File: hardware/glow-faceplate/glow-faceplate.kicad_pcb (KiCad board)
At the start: 2 copper layers, 80.9 x 68 mm, 15 parts

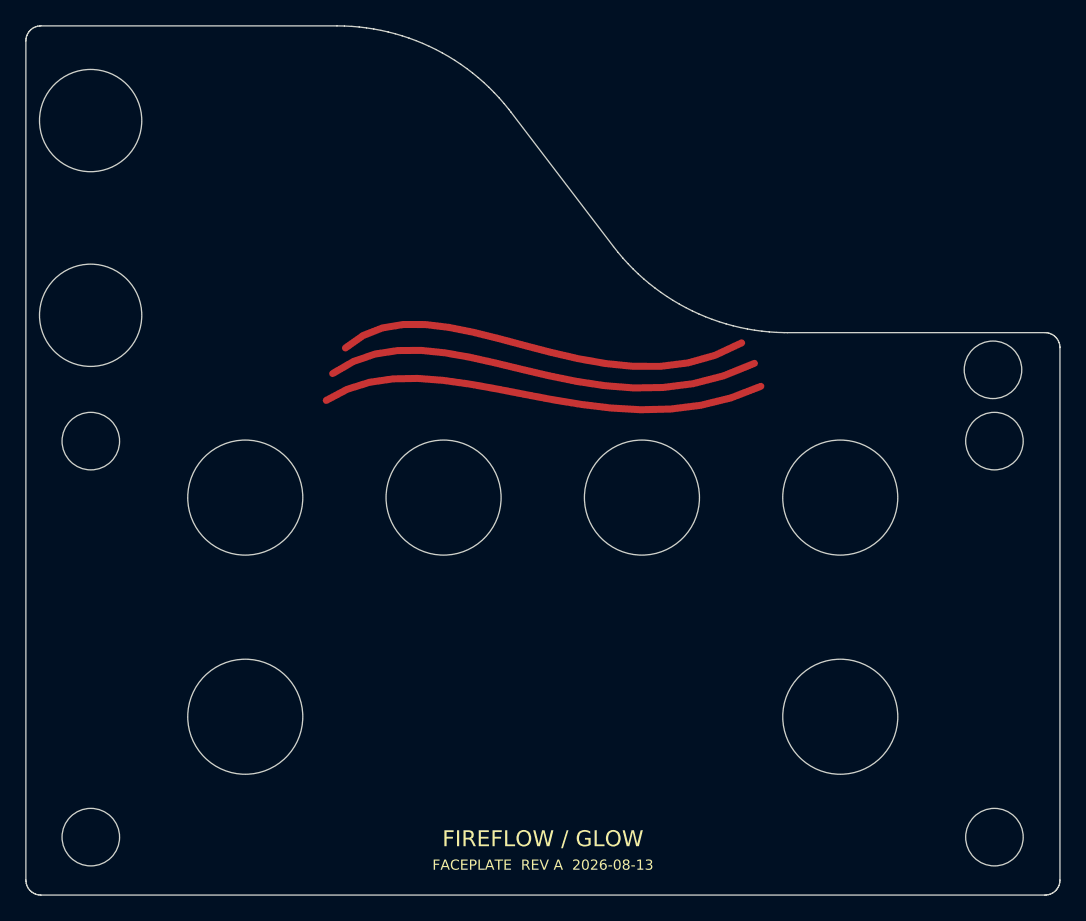
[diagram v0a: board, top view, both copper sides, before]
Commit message: fix(glow): derive faceplate mechanics from pinned DXF
Co-Authored-By: HAL 9000 <293417720+bea-ton-k@users.noreply.github.com>
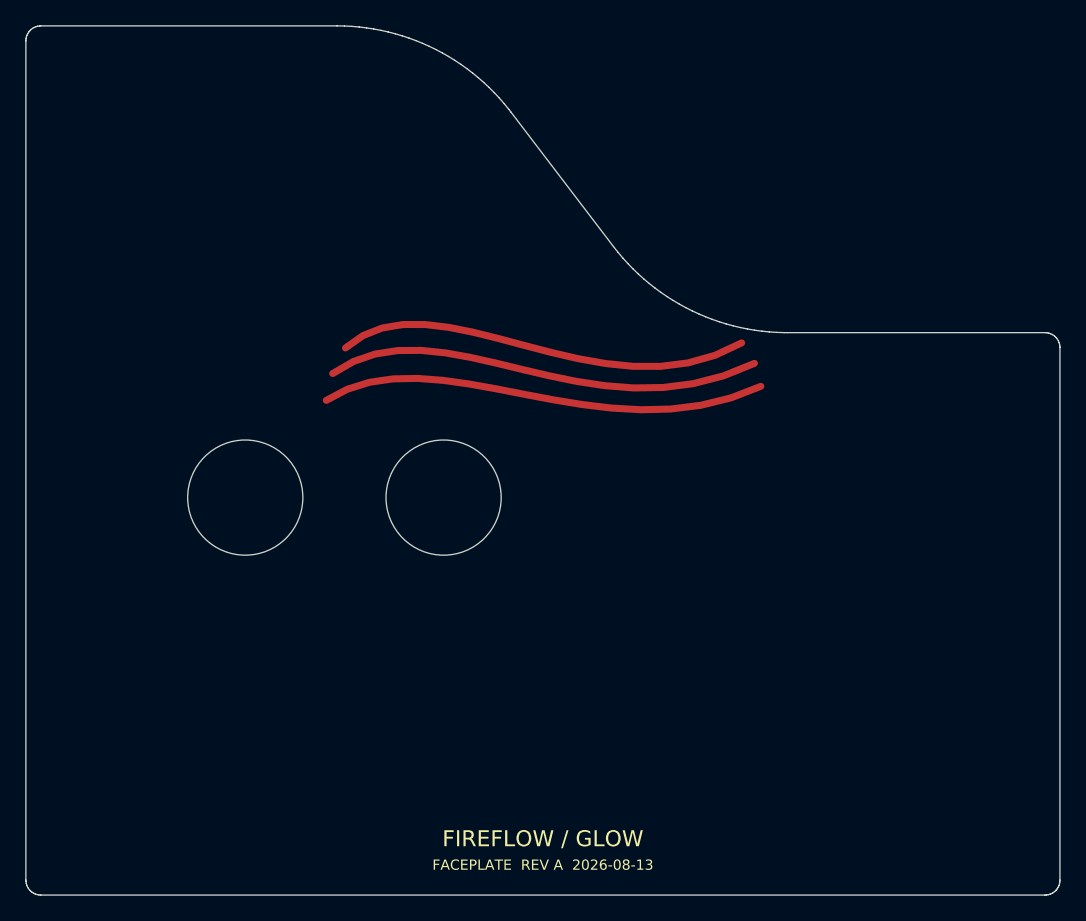
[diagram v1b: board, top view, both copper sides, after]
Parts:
- removed FADER_LEFT, FADER_RIGHT: NPTH SLOT 4.301 x 26.0409 mm, Glow_NPTH_SLOT_4.301x26.0409mm
- removed JACK_LOWER, JACK_UPPER: NPTH 8 mm, Glow_NPTH_8mm
- removed KNOB_1, KNOB_2, KNOB_3, KNOB_4, KNOB_5, KNOB_6: NPTH 9 mm, Glow_NPTH_9mm
- removed MOUNT_FADER_L_BOTTOM, MOUNT_FADER_L_TOP, MOUNT_FADER_R_BOTTOM, MOUNT_FADER_R_TOP, MOUNT_UPPER_RIGHT: NPTH 4.5 mm, Glow_NPTH_4.5mm
- added DXF_00: DXF NPTH 4.510605 x 4.528 mm, Glow_DXF_NPTH_DXF_00, F.Cu at (5.08, 32.5)
- added DXF_01_13_17: DXF NPTH 4.300995 x 26.0409 mm, Glow_DXF_NPTH_DXF_01_13_17, F.Cu at (5.08, 48.0)
- added DXF_02_12: DXF NPTH 9.010597 x 9.010597 mm, Glow_DXF_NPTH_DXF_02_12, F.Cu at (17.2, 36.9)
- added DXF_03_11: DXF NPTH 9.010597 x 9.010597 mm, Glow_DXF_NPTH_DXF_03_11, F.Cu at (32.7, 36.9)
- added DXF_04_10: DXF NPTH 9.010604 x 9.010601 mm, Glow_DXF_NPTH_DXF_04_10, F.Cu at (48.2, 36.8)
- added DXF_05_07_09: DXF NPTH 9.010604 x 9.010597 mm, Glow_DXF_NPTH_DXF_05_07_09, F.Cu at (63.7, 36.9)
- added DXF_06: DXF NPTH 4.510605 x 4.528 mm, Glow_DXF_NPTH_DXF_06, F.Cu at (75.8, 32.5)
- added DXF_08: DXF NPTH 4.300995 x 26.0409 mm, Glow_DXF_NPTH_DXF_08, F.Cu at (75.8, 48.0)
- added DXF_14_16: DXF NPTH 9.010597 x 9.010601 mm, Glow_DXF_NPTH_DXF_14_16, F.Cu at (17.2, 54.0)
- added DXF_15: DXF NPTH 9.010604 x 9.010601 mm, Glow_DXF_NPTH_DXF_15, F.Cu at (63.7, 54.0)
- added DXF_18: DXF NPTH 4.510605 x 4.528 mm, Glow_DXF_NPTH_DXF_18, F.Cu at (5.08, 63.5)
- added DXF_21: DXF NPTH 4.510605 x 4.528 mm, Glow_DXF_NPTH_DXF_21, F.Cu at (75.8, 63.5)
- added DXF_23: DXF NPTH 8.010597 x 8.0107 mm, Glow_DXF_NPTH_DXF_23, F.Cu at (5.07, 7.41)
- added DXF_24: DXF NPTH 8.010597 x 8.010702 mm, Glow_DXF_NPTH_DXF_24, F.Cu at (5.07, 22.6)
- added DXF_25: DXF NPTH 4.510589 x 4.510601 mm, Glow_DXF_NPTH_DXF_25, F.Cu at (75.7, 26.9)

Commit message: fix(glow): route exact DXF aperture contours
Co-Authored-By: HAL 9000 <293417720+bea-ton-k@users.noreply.github.com>
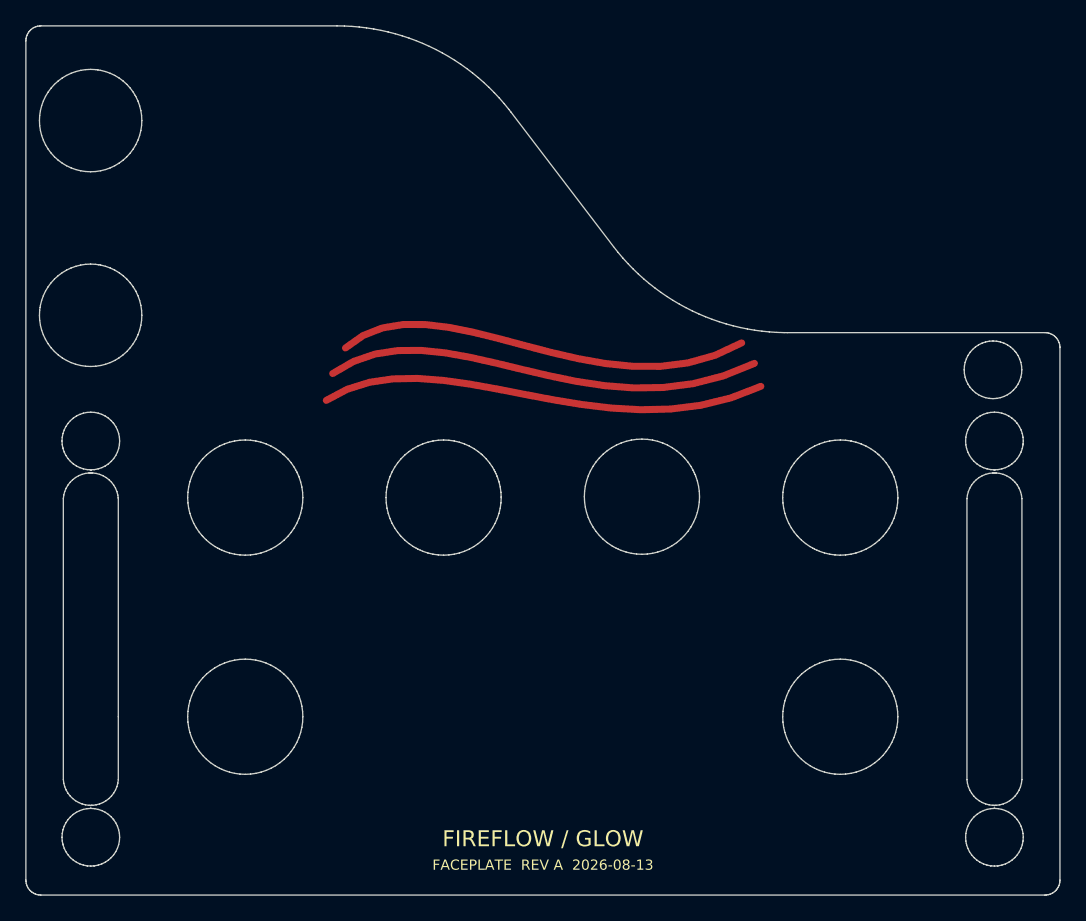
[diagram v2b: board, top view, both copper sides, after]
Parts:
- removed DXF_00: DXF NPTH 4.510605 x 4.528 mm, Glow_DXF_NPTH_DXF_00
- removed DXF_01_13_17: DXF NPTH 4.300995 x 26.0409 mm, Glow_DXF_NPTH_DXF_01_13_17
- removed DXF_02_12: DXF NPTH 9.010597 x 9.010597 mm, Glow_DXF_NPTH_DXF_02_12
- removed DXF_03_11: DXF NPTH 9.010597 x 9.010597 mm, Glow_DXF_NPTH_DXF_03_11
- removed DXF_04_10: DXF NPTH 9.010604 x 9.010601 mm, Glow_DXF_NPTH_DXF_04_10
- removed DXF_05_07_09: DXF NPTH 9.010604 x 9.010597 mm, Glow_DXF_NPTH_DXF_05_07_09
- removed DXF_06: DXF NPTH 4.510605 x 4.528 mm, Glow_DXF_NPTH_DXF_06
- removed DXF_08: DXF NPTH 4.300995 x 26.0409 mm, Glow_DXF_NPTH_DXF_08
- removed DXF_14_16: DXF NPTH 9.010597 x 9.010601 mm, Glow_DXF_NPTH_DXF_14_16
- removed DXF_15: DXF NPTH 9.010604 x 9.010601 mm, Glow_DXF_NPTH_DXF_15
- removed DXF_18: DXF NPTH 4.510605 x 4.528 mm, Glow_DXF_NPTH_DXF_18
- removed DXF_21: DXF NPTH 4.510605 x 4.528 mm, Glow_DXF_NPTH_DXF_21
- removed DXF_23: DXF NPTH 8.010597 x 8.0107 mm, Glow_DXF_NPTH_DXF_23
- removed DXF_24: DXF NPTH 8.010597 x 8.010702 mm, Glow_DXF_NPTH_DXF_24
- removed DXF_25: DXF NPTH 4.510589 x 4.510601 mm, Glow_DXF_NPTH_DXF_25
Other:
- outline, holes or cut-outs redrawn
